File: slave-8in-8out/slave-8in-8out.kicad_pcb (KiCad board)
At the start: 2 copper layers, 61 x 72.4 mm, 33 parts, among them J1 Conn_01x06_Male, J2 Screw_Terminal_01x02, J3 Conn_01x06_Female, J4 Screw_Terminal_01x04, J5 Screw_Terminal_01x04, J6 Screw_Terminal_01x04, J7 Screw_Terminal_01x04, J8 Conn_01x10_Male, J9 Screw_Terminal_01x02, SW1 SW_DIP_x03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

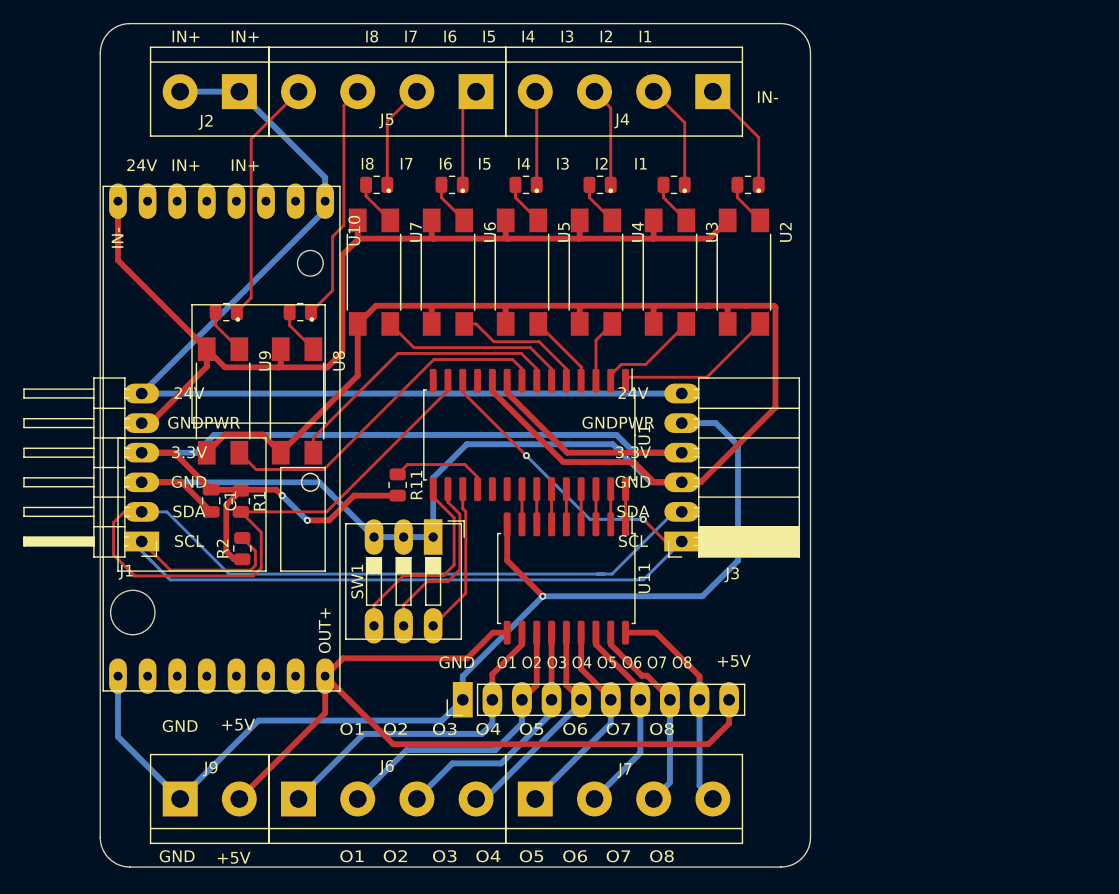
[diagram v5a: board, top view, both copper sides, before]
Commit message: refactor 8in-8out
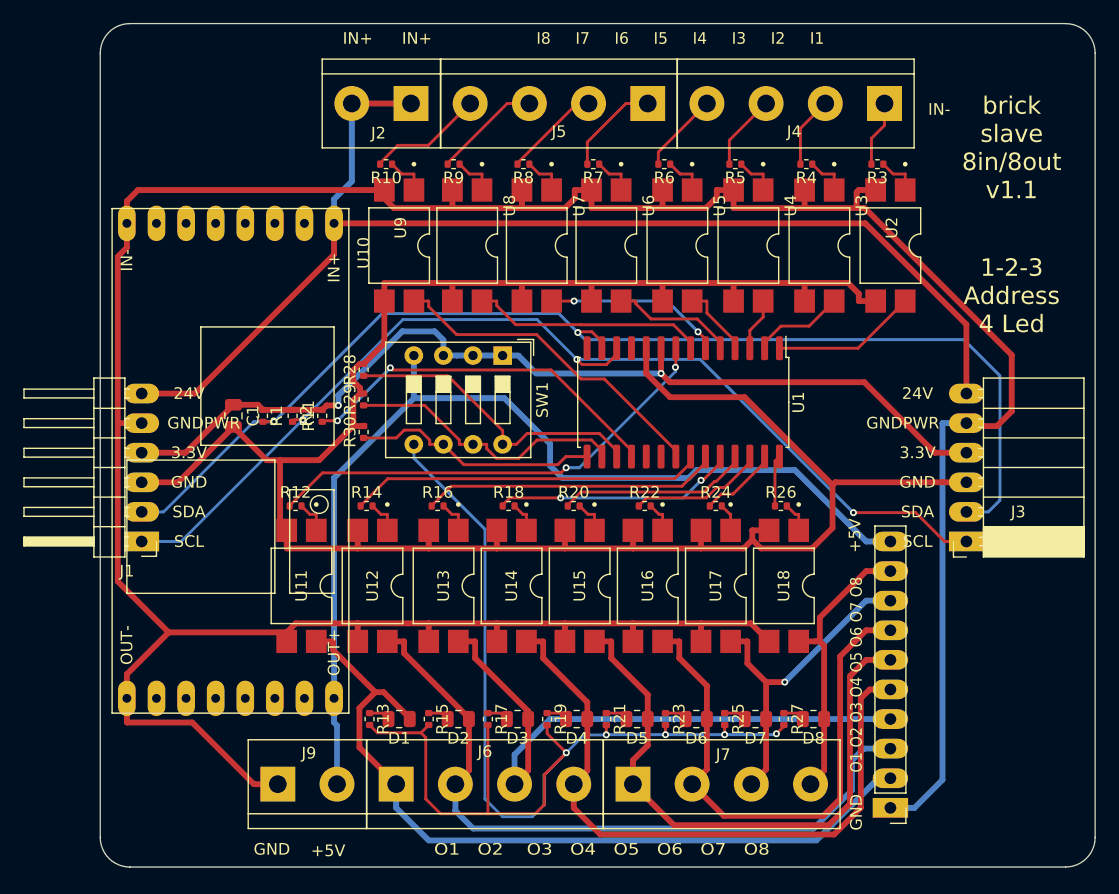
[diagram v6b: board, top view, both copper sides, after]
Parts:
- added D1: LED, Resistor_SMD:R_0805_2012Metric, F.Cu at (89.2, 114.3)
- added D2: LED, Resistor_SMD:R_0805_2012Metric, F.Cu at (94.2, 114.3)
- added D3: LED, Resistor_SMD:R_0805_2012Metric, F.Cu at (99.3, 114.3)
- added D4: LED, Resistor_SMD:R_0805_2012Metric, F.Cu at (104.4, 114.3)
- added D5: LED, Resistor_SMD:R_0805_2012Metric, F.Cu at (109.6, 114.3)
- added D6: LED, Resistor_SMD:R_0805_2012Metric, F.Cu at (114.7, 114.3)
- added D7: LED, Resistor_SMD:R_0805_2012Metric, F.Cu at (119.7, 114.3)
- added D8: LED, Resistor_SMD:R_0805_2012Metric, F.Cu at (124.7, 114.3)
- added R12: 680, Resistor_SMD:R_0402_1005Metric, F.Cu at (80.3, 96.0)
- added R13: 680, Resistor_SMD:R_0402_1005Metric, F.Cu at (86.6, 114.3)
- added R14: 680, Resistor_SMD:R_0402_1005Metric, F.Cu at (86.4, 96.0)
- added R15: 680, Resistor_SMD:R_0402_1005Metric, F.Cu at (91.7, 114.3)
- added R16: 680, Resistor_SMD:R_0402_1005Metric, F.Cu at (92.5, 96.0)
- added R17: 680, Resistor_SMD:R_0402_1005Metric, F.Cu at (96.8, 114.3)
- added R18: 680, Resistor_SMD:R_0402_1005Metric, F.Cu at (98.5, 96.0)
- added R19: 680, Resistor_SMD:R_0402_1005Metric, F.Cu at (101.9, 114.3)
- added R20: 680, Resistor_SMD:R_0402_1005Metric, F.Cu at (104.1, 96.0)
- added R21: 680, Resistor_SMD:R_0402_1005Metric, F.Cu at (106.9, 114.3)
- added R22: 680, Resistor_SMD:R_0402_1005Metric, F.Cu at (110.2, 96.0)
- added R23: 680, Resistor_SMD:R_0402_1005Metric, F.Cu at (112.0, 114.3)
- added R24: 680, Resistor_SMD:R_0402_1005Metric, F.Cu at (116.3, 96.0)
- added R25: 680, Resistor_SMD:R_0402_1005Metric, F.Cu at (117.1, 114.3)
- added R26: 680, Resistor_SMD:R_0402_1005Metric, F.Cu at (121.9, 96.0)
- added R27: 680, Resistor_SMD:R_0402_1005Metric, F.Cu at (122.2, 114.3)
- added R28: 10k, Resistor_SMD:R_0402_1005Metric, F.Cu at (86.1, 84.3)
- added R29: 10k, Resistor_SMD:R_0402_1005Metric, F.Cu at (86.1, 86.9)
- added R30: 10k, Resistor_SMD:R_0402_1005Metric, F.Cu at (86.1, 89.7)
- added U12: EL817, jlcpcb:EL817, F.Cu at (86.9, 102.9)
- added U13: EL817, jlcpcb:EL817, F.Cu at (93.0, 102.9)
- added U14: EL817, jlcpcb:EL817, F.Cu at (98.8, 102.9)
- added U15: EL817, jlcpcb:EL817, F.Cu at (104.6, 102.9)
- added U16: EL817, jlcpcb:EL817, F.Cu at (110.5, 102.9)
- added U17: EL817, jlcpcb:EL817, F.Cu at (116.3, 102.9)
- added U18: EL817, jlcpcb:EL817, F.Cu at (122.2, 102.9)
- R1, R10, R11, R2, R3, R4, R5, R6, R7, R8, R9: footprint Resistor_SMD:R_0805_2012Metric -> Resistor_SMD:R_0402_1005Metric
- SW1: value SW_DIP_x03 -> SW_DIP_x04; footprint Button_Switch_THT:SW_DIP_SPSTx03_Slide_9.78x9.8mm_W7.62mm_P2.54mm -> Button_Switch_THT:SW_DIP_SPSTx04_Slide_9.78x12.34mm_W7.62mm_P2.54mm
- U11: value ULN2803A -> EL817; footprint Package_SO:SOIC-18W_7.5x11.6mm_P1.27mm -> jlcpcb:EL817
- moved J8 37.9 mm to (131.3, 121.9), turned to 180 degrees
- moved J3 24.4 mm to (137.8, 99.1)
- moved U11 22.7 mm to (80.8, 102.9)
- moved U9 20.2 mm to (89.2, 73.7)
- moved U8 19.8 mm to (95.0, 73.7)
- moved R10 18.7 mm to (88.0, 66.7), turned to 180 degrees
- moved R9 18.3 mm to (93.8, 66.7), turned to 180 degrees
- moved SW1 16.7 mm to (98.0, 83.1)
- moved J2 14.8 mm to (90.2, 61.5)
- moved J4 14.8 mm to (130.8, 61.5)
- moved J5 14.8 mm to (110.5, 61.5)
- moved U7 14.2 mm to (101.0, 73.7)
- moved U6 13.8 mm to (106.9, 73.7)
- moved U5 13.5 mm to (113.0, 73.7)
- moved U1 13.5 mm to (113.5, 87.1)
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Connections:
- SW1 pad 1: GND -> +3V3
- SW1 pad 2: GND -> +3V3
- SW1 pad 3: GND -> +3V3
- SW1 pad 4: Net-(SW1-Pad4) -> +5V
- SW1 pad 5: Net-(SW1-Pad5) -> LED_PWR
- SW1 pad 6: Net-(SW1-Pad6) -> A0
- U1 pad 11: Net-(U1-Pad11) -> unconnected-(U1-Pad11)
- U1 pad 14: Net-(U1-Pad14) -> unconnected-(U1-Pad14)
- U1 pad 15: Net-(SW1-Pad4) -> A0
- U1 pad 16: Net-(SW1-Pad5) -> A1
- U1 pad 17: Net-(SW1-Pad6) -> A2
- U1 pad 19: Net-(U1-Pad19) -> unconnected-(U1-Pad19)
- U1 pad 20: Net-(U1-Pad20) -> unconnected-(U1-Pad20)
- U11 pad 1: GPA7 -> Net-(R12-Pad2)
- U11 pad 2: GPA6 -> GND
- U11 pad 3: GPA5 -> GNDPWR
- U11 pad 4: GPA4 -> O1
- U9 pad 4: GPB7 -> GPA0
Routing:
- net LED_PWR: track 0.00 -> 105.0 mm, vias 0 -> 5
- net GNDPWR: track 183.9 -> 273.0 mm, vias 1 -> 0
- net O1: track 28.2 -> 68.8 mm
- net O4: track 19.0 -> 56.6 mm
- net O2: track 25.1 -> 61.1 mm
- net O5: track 18.0 -> 51.4 mm
- net O3: track 21.5 -> 52.1 mm
- net O6: track 17.5 -> 47.1 mm
- net GPA1: track 3.02 -> 30.4 mm
- net A2: track 0.00 -> 26.3 mm
- net GND: track 169.0 -> 195.2 mm
- net GPA0: track 3.02 -> 28.6 mm
- net A1: track 0.00 -> 24.3 mm
- net Net-(U1-Pad18): track 8.68 -> 31.9 mm, vias 0 -> 2
- net GPA2: track 3.02 -> 25.6 mm
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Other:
- board size 61 x 72.4 mm -> 85.4 x 72.4 mm
- board text added: "1-2-3 Address 4 Led"
- board text added: "brick slave 8in/8out v1.1"

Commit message: refactor slave-8in-8out
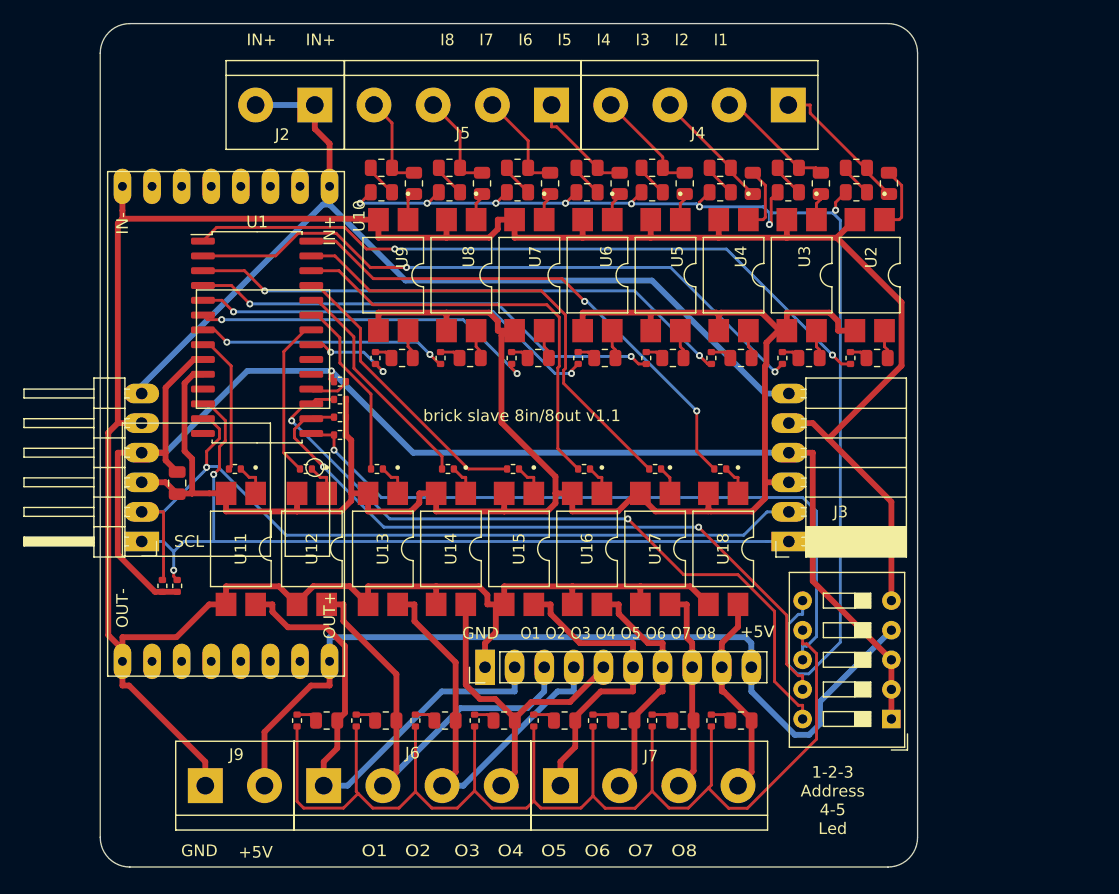
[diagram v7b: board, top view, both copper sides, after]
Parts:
- added D10: LED, Resistor_SMD:R_0805_2012Metric, F.Cu at (130.2, 83.3)
- added D11: LED, Resistor_SMD:R_0805_2012Metric, F.Cu at (122.6, 69.1)
- added D12: LED, Resistor_SMD:R_0805_2012Metric, F.Cu at (124.3, 83.3)
- added D13: LED, Resistor_SMD:R_0805_2012Metric, F.Cu at (116.7, 69.1)
- added D14: LED, Resistor_SMD:R_0805_2012Metric, F.Cu at (118.5, 83.3)
- added D15: LED, Resistor_SMD:R_0805_2012Metric, F.Cu at (110.9, 69.1)
- added D16: LED, Resistor_SMD:R_0805_2012Metric, F.Cu at (112.6, 83.3)
- added D17: LED, Resistor_SMD:R_0805_2012Metric, F.Cu at (105.3, 69.1)
- added D18: LED, Resistor_SMD:R_0805_2012Metric, F.Cu at (106.8, 83.3)
- added D19: LED, Resistor_SMD:R_0805_2012Metric, F.Cu at (99.3, 69.1)
- added D20: LED, Resistor_SMD:R_0805_2012Metric, F.Cu at (101.1, 83.3)
- added D21: LED, Resistor_SMD:R_0805_2012Metric, F.Cu at (93.5, 69.1)
- added D22: LED, Resistor_SMD:R_0805_2012Metric, F.Cu at (95.2, 83.3)
- added D23: LED, Resistor_SMD:R_0805_2012Metric, F.Cu at (87.6, 69.1)
- added D24: LED, Resistor_SMD:R_0805_2012Metric, F.Cu at (89.4, 83.3)
- added D9: LED, Resistor_SMD:R_0805_2012Metric, F.Cu at (128.4, 69.1)
- added R31: 330, Resistor_SMD:R_0402_1005Metric, F.Cu at (116.0, 83.3)
- added R32: 4k7, Resistor_SMD:R_0805_2012Metric, F.Cu at (110.9, 67.0)
- added R33: 4k7, Resistor_SMD:R_0805_2012Metric, F.Cu at (113.7, 68.3)
- added R34: 330, Resistor_SMD:R_0402_1005Metric, F.Cu at (110.4, 83.3)
- added R35: 4k7, Resistor_SMD:R_0805_2012Metric, F.Cu at (105.3, 67.0)
- added R36: 4k7, Resistor_SMD:R_0805_2012Metric, F.Cu at (108.1, 68.3)
- added R37: 330, Resistor_SMD:R_0402_1005Metric, F.Cu at (104.5, 83.3)
- added R38: 4k7, Resistor_SMD:R_0805_2012Metric, F.Cu at (99.3, 67.0)
- added R39: 4k7, Resistor_SMD:R_0805_2012Metric, F.Cu at (102.1, 68.3)
- added R40: 330, Resistor_SMD:R_0402_1005Metric, F.Cu at (98.8, 83.3)
- added R41: 4k7, Resistor_SMD:R_0805_2012Metric, F.Cu at (93.5, 67.0)
- added R42: 4k7, Resistor_SMD:R_0805_2012Metric, F.Cu at (96.3, 68.3)
- added R43: 330, Resistor_SMD:R_0402_1005Metric, F.Cu at (92.7, 83.3)
- added R44: 4k7, Resistor_SMD:R_0805_2012Metric, F.Cu at (87.6, 67.0)
- added R45: 4k7, Resistor_SMD:R_0805_2012Metric, F.Cu at (90.4, 68.3)
- added R46: 330, Resistor_SMD:R_0402_1005Metric, F.Cu at (87.1, 83.3)
- R10, R3, R4, R6, R7, R9: footprint Resistor_SMD:R_0402_1005Metric -> Resistor_SMD:R_0805_2012Metric
- R5, R8: value 4k7 -> 330
- SW1: value SW_DIP_x04 -> SW_DIP_x05; footprint Button_Switch_THT:SW_DIP_SPSTx04_Slide_9.78x12.34mm_W7.62mm_P2.54mm -> Button_Switch_THT:SW_DIP_SPSTx05_Slide_9.78x14.88mm_W7.62mm_P2.54mm
- moved SW1 45.7 mm to (131.4, 114.3), turned to 180 degrees
- moved U1 37.0 mm to (77.0, 81.5), turned to 0 degrees
- moved J8 36.8 mm to (96.5, 109.9), turned to 90 degrees
- moved R10 31.5 mm to (119.5, 68.3), turned to -90 degrees
- moved R8 27.8 mm to (122.0, 83.3), turned to 90 degrees
- moved R9 22.9 mm to (116.7, 67.0)
- moved R7 19.6 mm to (125.3, 68.3), turned to 90 degrees
- moved R5 19.4 mm to (127.9, 83.3), turned to 90 degrees
- moved R2 17.6 mm to (70.1, 102.9), turned to 90 degrees
- moved R1 17.0 mm to (68.8, 102.9), turned to 90 degrees
- moved J3 15.2 mm to (122.6, 99.1)
- moved R6 10.6 mm to (122.6, 67.0)
- moved J2 8.26 mm to (81.9, 61.6)
- moved J4 8.26 mm to (122.6, 61.6)
- moved J5 8.26 mm to (102.2, 61.6)
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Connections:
- R10 pad 2: I8 -> I3
- R3 pad 1: Net-(R3-Pad1) -> I1
- R3 pad 2: I1 -> Net-(D9-Pad2)
- R4 pad 2: I2 -> I1
- R5 pad 1: Net-(R5-Pad1) -> GPB0
- R5 pad 2: I3 -> Net-(D10-Pad2)
- R6 pad 1: Net-(R6-Pad1) -> I2
- R6 pad 2: I4 -> Net-(D11-Pad2)
- R7 pad 2: I5 -> I2
- R8 pad 1: Net-(R8-Pad1) -> GPB1
- R8 pad 2: I6 -> Net-(D12-Pad2)
- R9 pad 1: Net-(R9-Pad1) -> I3
- R9 pad 2: I7 -> Net-(D13-Pad2)
- SW1 pad 5: LED_PWR -> GNDPWR
- SW1 pad 6: A0 -> LED_GNDPWR
- SW1 pad 7: A1 -> LED_PWR
- SW1 pad 8: A2 -> A0
- U2 pad 1: Net-(R3-Pad1) -> Net-(R4-Pad1)
- U2 pad 4: GPB0 -> Net-(D10-Pad1)
- U3 pad 1: Net-(R4-Pad1) -> Net-(R7-Pad1)
- U3 pad 4: GPB1 -> Net-(D12-Pad1)
- U4 pad 1: Net-(R5-Pad1) -> Net-(R10-Pad1)
- U4 pad 4: GPB2 -> Net-(D14-Pad1)
- U5 pad 1: Net-(R6-Pad1) -> Net-(R33-Pad1)
- U5 pad 4: GPB3 -> Net-(D16-Pad1)
- U6 pad 1: Net-(R7-Pad1) -> Net-(R36-Pad1)
- U6 pad 4: GPB4 -> Net-(D18-Pad1)
- U7 pad 1: Net-(R8-Pad1) -> Net-(R39-Pad1)
- U7 pad 4: GPB5 -> Net-(D20-Pad1)
- U8 pad 1: Net-(R9-Pad1) -> Net-(R42-Pad1)
- U8 pad 4: GPB6 -> Net-(D22-Pad1)
- U9 pad 1: Net-(R10-Pad1) -> Net-(R45-Pad1)
- U9 pad 4: GPA0 -> Net-(D24-Pad1)
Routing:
- net LED_GNDPWR: track 0.00 -> 104.8 mm, vias 0 -> 8
- net GPB0: track 12.5 -> 60.9 mm, vias 0 -> 2
- net GPB1: track 7.94 -> 55.8 mm, vias 0 -> 2
- net GPB2: track 4.52 -> 47.0 mm, vias 0 -> 2
- net GPA7: track 4.40 -> 44.7 mm, vias 0 -> 2
- net A0: track 21.2 -> 60.3 mm, vias 0 -> 1
- net +3V3: track 83.2 -> 121.2 mm, vias 2 -> 1
- net A2: track 26.3 -> 63.2 mm, vias 0 -> 2
- net A1: track 24.3 -> 60.3 mm, vias 0 -> 2
- net GPB3: track 6.31 -> 40.8 mm, vias 0 -> 2
- net GPA6: track 6.78 -> 40.2 mm
- net O4: track 56.6 -> 28.0 mm
- net Net-(R11-Pad1): track 31.9 -> 3.43 mm, vias 2 -> 0
- net GPB7: track 39.9 -> 12.1 mm, vias 2 -> 0
- net SDA: track 100.8 -> 73.8 mm, vias 2 -> 1
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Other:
- board size 85.4 x 72.4 mm -> 70.1 x 72.4 mm
- board text added: "1-2-3 Address 4-5 Led"
- board text removed: "1-2-3 Address 4 Led"
- board text removed: "24V"
- board text removed: "3.3V"
- board text removed: "GNDPWR"
- board text removed: "IN-"
- board text removed: "SDA"

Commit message: refactor slave-8in-8out
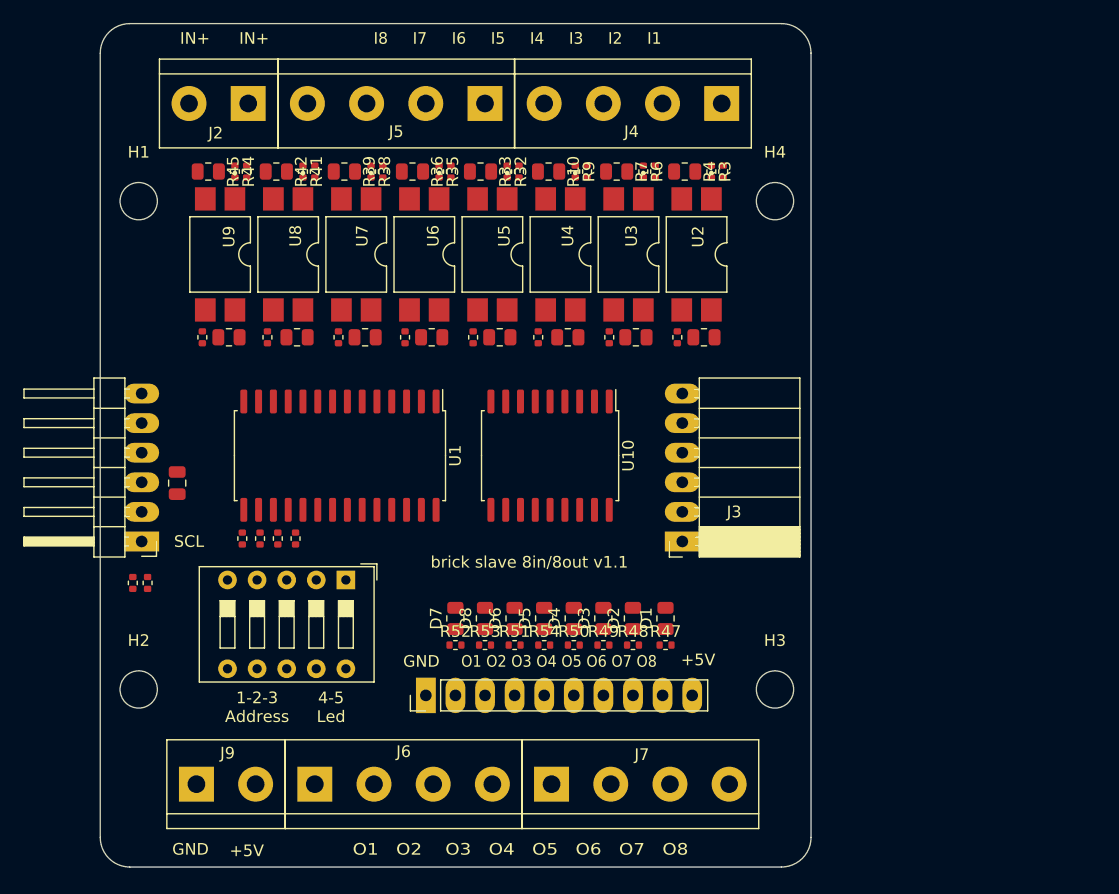
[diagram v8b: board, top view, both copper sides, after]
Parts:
- removed R12, R13, R14, R15, R16, R17, R18, R19, R20, R21, R22, R23, R24, R25, R26, R27: 680, Resistor_SMD:R_0402_1005Metric
- removed U11, U12, U13, U14, U15, U16, U17, U18: EL817, jlcpcb:EL817
- added H1: MountingHole, MountingHole:MountingHole_3.2mm_M3, F.Cu at (66.8, 69.8)
- added H2: MountingHole, MountingHole:MountingHole_3.2mm_M3, F.Cu at (66.8, 111.8)
- added H3: MountingHole, MountingHole:MountingHole_3.2mm_M3, F.Cu at (121.4, 111.8)
- added H4: MountingHole, MountingHole:MountingHole_3.2mm_M3, F.Cu at (121.4, 69.8)
- added R47: 330, Resistor_SMD:R_0402_1005Metric, F.Cu at (112.0, 108.0)
- added R48: 330, Resistor_SMD:R_0402_1005Metric, F.Cu at (109.2, 108.0)
- added R49: 330, Resistor_SMD:R_0402_1005Metric, F.Cu at (106.7, 108.0)
- added R50: 330, Resistor_SMD:R_0402_1005Metric, F.Cu at (104.1, 108.0)
- added R51: 330, Resistor_SMD:R_0402_1005Metric, F.Cu at (99.1, 108.0)
- added R52: 330, Resistor_SMD:R_0402_1005Metric, F.Cu at (94.0, 108.0)
- added R53: 330, Resistor_SMD:R_0402_1005Metric, F.Cu at (96.5, 108.0)
- added R54: 330, Resistor_SMD:R_0402_1005Metric, F.Cu at (101.6, 108.0)
- R10, R3, R32, R33, R35, R36, R38, R39, R4, R41, R42, R44, R45, R6, R7, R9: value 4k7 -> 680; footprint Resistor_SMD:R_0805_2012Metric -> Resistor_SMD:R_0402_1005Metric
- U10: value LM2596-Board -> ULN2803A; footprint boards:LM2596-Board -> Package_SO:SOIC-18W_7.5x11.6mm_P1.27mm
- moved SW1 48.3 mm to (84.6, 102.4), turned to -90 degrees
- moved D1 30.4 mm to (112.0, 105.7), turned to 90 degrees
- moved U10 28.0 mm to (102.1, 91.7)
- moved D8 23.7 mm to (96.5, 105.7), turned to 90 degrees
- moved D2 22.9 mm to (109.2, 105.7), turned to 90 degrees
- moved D7 21.4 mm to (94.0, 105.7), turned to 90 degrees
- moved D3 16.2 mm to (106.7, 105.7), turned to 90 degrees
- moved D17 15.1 mm to (90.3, 67.3)
- moved D10 15.0 mm to (115.3, 81.5)
- moved D18 15.0 mm to (91.9, 81.5)
- moved U2 15.0 mm to (114.7, 74.4)
- moved U3 15.0 mm to (108.8, 74.4)
- moved U4 15.0 mm to (103.0, 74.4)
- moved U5 15.0 mm to (97.2, 74.4)
- moved U6 15.0 mm to (91.3, 74.4)
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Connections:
- D1 pad 1: O1 -> Net-(D1-Pad1)
- D1 pad 2: Net-(D1-Pad2) -> GPA7
- D2 pad 1: O2 -> Net-(D2-Pad1)
- D2 pad 2: Net-(D2-Pad2) -> GPA6
- D3 pad 1: O3 -> Net-(D3-Pad1)
- D3 pad 2: Net-(D3-Pad2) -> GPA5
- D4 pad 1: O4 -> Net-(D4-Pad1)
- D4 pad 2: Net-(D4-Pad2) -> GPA4
- D5 pad 1: O5 -> Net-(D5-Pad1)
- D5 pad 2: Net-(D5-Pad2) -> GPA3
- D6 pad 1: O6 -> Net-(D6-Pad1)
- D6 pad 2: Net-(D6-Pad2) -> GPA2
- D7 pad 1: O7 -> Net-(D7-Pad1)
- D7 pad 2: Net-(D7-Pad2) -> GPB7
- D8 pad 1: O8 -> Net-(D8-Pad1)
- D8 pad 2: Net-(D8-Pad2) -> GPA1
- J1 pad 6: +24V -> +5V
- J2 pad 1: +24V -> +5V
- J2 pad 2: +24V -> +5V
- J3 pad 6: +24V -> +5V
- SW1 pad 4: +5V -> GND
- SW1 pad 7: LED_PWR -> LED_GND
- U10 pad 1: +24V -> GPA7
- U10 pad 2: GNDPWR -> GPA6
- U10 pad 3: GNDPWR -> GPA5
- U10 pad 4: +5V -> GPA4
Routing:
- net GNDPWR: track 246.8 -> 0.00 mm
- net GND: track 170.1 -> 0.00 mm
- net +3V3: track 121.2 -> 0.00 mm, vias 1 -> 0
- net LED_PWR: track 111.4 -> 0.00 mm
- net LED_GNDPWR: track 104.8 -> 0.00 mm, vias 8 -> 0
- net +24V: track 83.5 -> 0.00 mm
- net +5V: track 75.0 -> 0.00 mm
- net SDA: track 73.8 -> 0.00 mm, vias 1 -> 0
- net SCL: track 72.1 -> 0.00 mm, vias 2 -> 0
- net A2: track 63.2 -> 0.00 mm, vias 2 -> 0
- net GPB0: track 60.9 -> 0.00 mm, vias 2 -> 0
- net A0: track 60.3 -> 0.00 mm, vias 1 -> 0
- net A1: track 60.3 -> 0.00 mm, vias 2 -> 0
- net GPB1: track 55.8 -> 0.00 mm, vias 2 -> 0
- net GPB2: track 47.0 -> 0.00 mm, vias 2 -> 0
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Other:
- board size 70.1 x 72.4 mm -> 61 x 72.4 mm
- board text added: "1-2-3 Address"
- board text added: "4-5 Led"
- board text removed: "1-2-3 Address 4-5 Led"
